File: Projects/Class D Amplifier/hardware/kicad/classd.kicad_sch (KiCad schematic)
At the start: 61 parts, among them J1 PWR IN 12V, J2 LINE IN, J3 SPEAKER 4R, Q1 IRF540N, Q2 IRF540N, Q3 IRF540N, Q4 IRF540N, U1 TL074, U2 LM311, U3 LM311, U4 LM311, U5 CD4049UBE, U6 HIP4082IPZ

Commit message: Class D amp: assign footprints, move to A2, and fix the sub crossover netclass
Every part now carries a through-hole footprint chosen for isolation milling
with an 0.8 mm end mill. The sheet moves to A2 to match how the board is being
drawn, and the layout script emits that so regenerating cannot revert it.

Footprints were audited for their smallest pad-to-pad gap before assignment,
because a gap narrower than the tool is never isolated and ships as a short.
Two stock picks failed that test. The Alps RK09K pot is 0.70 mm and cannot be
built, so the level control uses the ACP CA14V-15 with its 5 mm pin pitch
instead - the shop only specifies "10k", so measure the real part before
cutting copper. The stock TO-220 is 0.64 mm, so the bridge FETs use the
narrowed-pad variant at 0.84 mm; that clears the tool but sits under the
netclass clearance, so classd.kicad_dru relaxes it for those four parts and
nothing else. Everything else is 0.94 mm or wider.

The bornier terminal blocks and the mill-specific TO-220, LED and hand-wound
toroid footprints are vendored into lib/ and registered in fp-lib-table, since
KiCad 10 ships none of them.

subxo.kicad_pro gets the same netclass wire_width fix as this board. Its
Default class had no wire_width either, which is what makes KiCad 10 draw
every schematic wire at zero width and drop all the junction dots.
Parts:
- C1: footprint (none) -> Capacitor_THT:CP_Radial_D8.0mm_P3.50mm
- C10, C11, C12, C2, C5, C6, C7, C8, C9: footprint (none) -> Capacitor_THT:C_Disc_D5.0mm_W2.5mm_P5.00mm
- C13: footprint (none) -> Capacitor_THT:C_Rect_L16.5mm_W5.0mm_P15.00mm_MKT
- C14: footprint (none) -> Capacitor_THT:C_Rect_L7.0mm_W3.5mm_P5.00mm
- C3: footprint (none) -> Capacitor_THT:C_Rect_L13.0mm_W5.0mm_P10.00mm_FKS3_FKP3_MKS4
- C4: footprint (none) -> Capacitor_THT:CP_Radial_D18.0mm_P7.50mm
- D1: footprint (none) -> energy_system:LED_D3.0mm_P5.08mm_LaserPads
- D2, D3: footprint (none) -> Diode_THT:D_DO-41_SOD81_P10.16mm_Horizontal
- J1, J2, J3: footprint (none) -> TerminalBlock:TerminalBlock_bornier-2_P5.08mm
- L1, L2: footprint (none) -> energy_system:L_Toroid_Vertical_L34.5mm_W15.0mm_P28.20mm_LaserPads
- Q1, Q2, Q3, Q4: footprint (none) -> energy_system:TO-220-3_Vertical_LaserPads
- R1, R10, R11, R12, R13, R14, R15, R16, R17, R18, R19, R2, R20, R21, R3, R4, R5, R6, R7, R8, R9: footprint (none) -> Resistor_THT:R_Axial_DIN0207_L6.3mm_D2.5mm_P7.62mm_Horizontal
- R22: footprint (none) -> Resistor_THT:R_Axial_Power_L25.0mm_W9.0mm_P30.48mm
- RV1: footprint (none) -> Potentiometer_THT:Potentiometer_Bourns_3296W_Vertical
- RV2: footprint (none) -> Potentiometer_THT:Potentiometer_ACP_CA14V-15_Vertical
- TP1, TP2, TP3, TP4, TP5: footprint (none) -> TestPoint:TestPoint_THTPad_2.5x2.5mm_Drill1.2mm
- U1: footprint (none) -> Package_DIP:DIP-14_W7.62mm_LongPads
- U2, U3, U4: footprint (none) -> Package_DIP:DIP-8_W7.62mm_LongPads
- U5, U6: footprint (none) -> Package_DIP:DIP-16_W7.62mm_LongPads

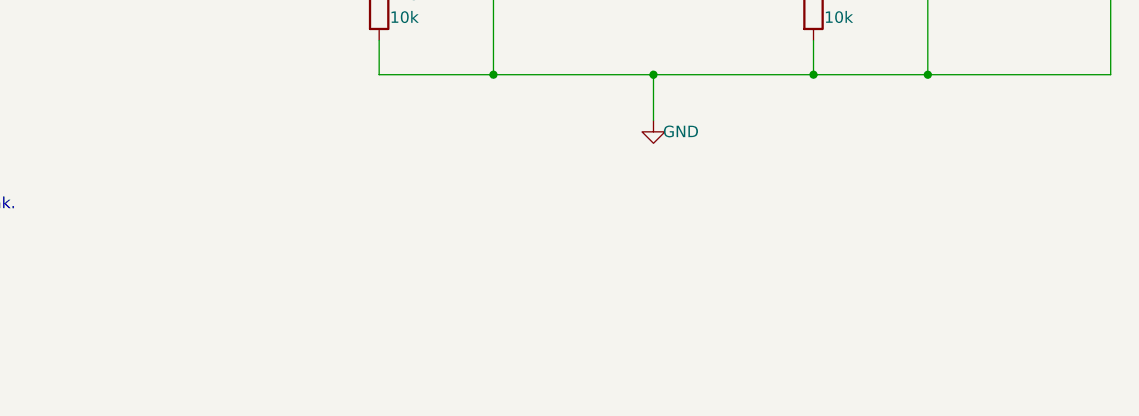
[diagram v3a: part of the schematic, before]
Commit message: Class D amp: link the testbenches from the board sheet, both ways
The board schematic now carries a SIMULATION index in the free space below the
bridge: one clickable line per testbench, opening that testbench's project.
Each testbench carries a link back to the board.

These are hyperlinks, not hierarchical sheets, and that was not the first
choice - it is the result of trying the obvious thing and measuring what it
did. Attaching sim_b_triangle to classd.kicad_sch as a hierarchical sheet and
exporting the netlist showed three separate kinds of damage: the testbench's
12 V source welded straight onto the board's +12V rail, taking it from 23 pins
to 25; the sim's sources landing in the board netlist ready for Update PCB
from Schematic to push them onto copper; and worst, the sim sheet's U1, R4 and
R5 silently merging with the board parts of the same name, quietly rewiring
real components. A hierarchy is one electrical design, so anything inside it
is part of the board whether you meant it or not.

Getting the hyperlink right took measuring too. KiCad 10 refuses to load a
schematic where the link is spelled (hyperlink ...) as it is on the PCB, or
where it sits beside (uuid ...) rather than inside (effects ...). It also
rejects an href that is a bare relative path or a ${KIPRJMOD} variable, but
accepts a relative path carrying the file: scheme - which is what is used, so
the links survive the repository being checked out anywhere.

Also fixed while here: labels that sat beside a wire end rather than on it
left dangling endpoints, and the testbench supplies needed a ground PWR_FLAG
as well as a rail one. All four sheets now pass ERC with zero violations, and
the simulation checks still pass 16/16.
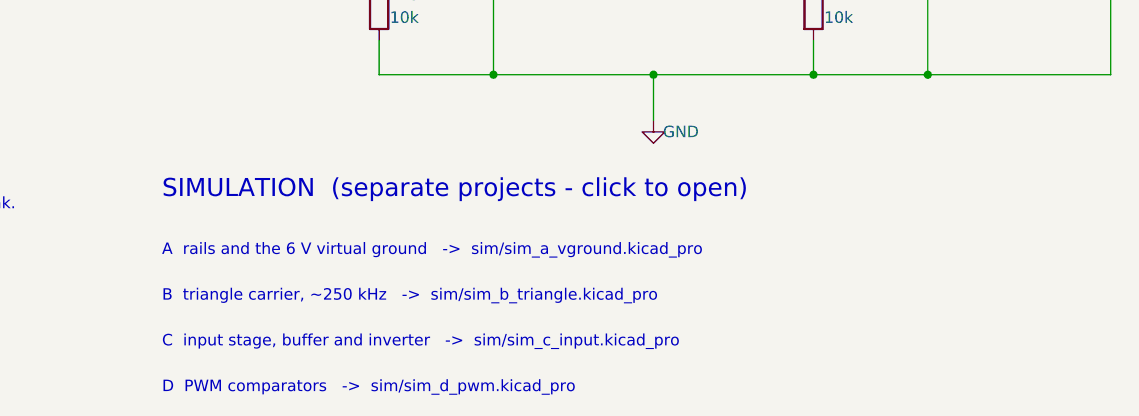
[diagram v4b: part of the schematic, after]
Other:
- note added: "A rails and the 6 V virtual ground -> sim/sim_a_vground.kicad_pro"
- note added: "B triangle carrier, ~250 kHz -> sim/sim_b_triangle.kicad_pro"
- note added: "C input stage, buffer and inverter -> sim/sim_c_input.kicad_pro"
- note added: "D PWM comparators -> sim/sim_d_pwm.kicad_pro"
- note added: "SIMULATION (separate projects - click to open)"
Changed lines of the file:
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@@
+		)
+	)
+	(text "SIMULATION  (separate projects - click to open)"
+		(at 317.5 374.65 0)
+		(effects
+			(font
+				(size 2 2)
+			)
+			(justify left bottom)
+		)
+	)
+	(text "A  rails and the 6 V virtual ground   ->  sim/sim_a_vground.kicad_pro"
+		(at 317.5 381 0)
+		(effects
+			(font
+				(size 1.27 1.27)
+			)
+			(justify left bottom)
+			(href "file:sim/sim_a_vground.kicad_pro")
+		)
+	)
+	(text "B  triangle carrier, ~250 kHz   ->  sim/sim_b_triangle.kicad_pro"
+		(at 317.5 386.08 0)
+		(effects
+			(font
+				(size 1.27 1.27)
+			)
+			(justify left bottom)
+			(href "file:sim/sim_b_triangle.kicad_pro")
+		)
+	)
+	(text "C  input stage, buffer and inverter   ->  sim/sim_c_input.kicad_pro"
+		(at 317.5 391.16 0)
+		(effects
+			(font
+				(size 1.27 1.27)
+			)
+			(justify left bottom)
+			(href "file:sim/sim_c_input.kicad_pro")
+		)
+	)
+	(text "D  PWM comparators   ->  sim/sim_d_pwm.kicad_pro"
+		(at 317.5 396.24 0)
+		(effects
+			(font
+				(size 1.27 1.27)
+			)
+			(justify left bottom)
+			(href "file:sim/sim_d_pwm.kicad_pro")
 		)
 	)

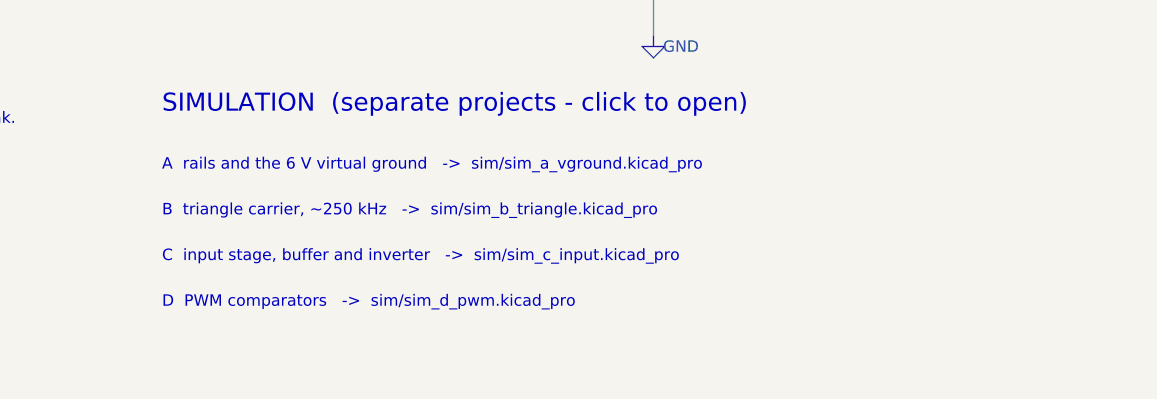
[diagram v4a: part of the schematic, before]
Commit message: Class D amp: the remaining three testbenches, E, F and G
E drives the CD4049 complement chain into the HIP4082 and measures what the
dead-time resistor actually buys: 225 ns with both gates off, never both on,
and a bootstrap that fills in ~50 us and settles one Schottky drop below the
rail. The switch nodes need holding down for that -- left floating they drift
up through the driver's own leakage until the bootstrap caps have barely a
volt across them, so R23/R24 stand in for the low-side FET being on.

F puts four real IRF540N cards, body diode included, under the driver and runs
them into the LC filter and a 4 ohm load at a fixed 79/21 duty: 11.75 W with
0.28 Vpp of carrier left on the output.

G is the whole chain, audio in to speaker out, and it is the one that answers
the design question. It makes 13 W -- and at that level AUDIO_P bottoms out at
4.00 V, which is the TL074's input common-mode floor. Full output and the
input stage's limit coincide exactly; there is no headroom to trade. That was
flagged on paper in the build notes and is now a number the harness asserts.

Three fixes fell out of building them, all in code that had never been
exercised because no bench used it before:

- the IRF540N Sim.Pins map said 1=D 2=G, but the symbol numbers its pins to
  the TO-220 pinout, 1=G 2=D. The bridge would have simulated as four
  transistors wired gate to drain.
- KiCad validates every Sim.Params key against the subcircuit's own parameter
  list and refuses the netlist export for one it cannot find, so the HIP4082's
  dead time moves from an internal .param to the .subckt line.
- a sym-lib-table registers the vendored CD4049 symbol, clearing the
  lib_symbol_issues ERC violations on every sheet that uses it.

The driver, bridge and filter are now drawn once and translated onto the three
sheets, with the geometry taken from the matching block of the board's own
layout script -- a bootstrap wired one way on the board and another way in its
testbench proves nothin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
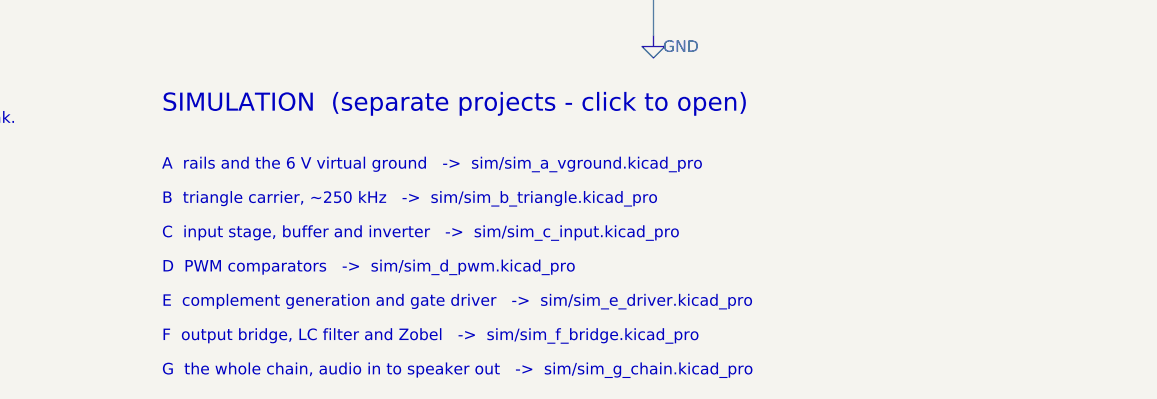
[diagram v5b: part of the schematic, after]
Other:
- note added: "E complement generation and gate driver -> sim/sim_e_driver.kicad_pro"
- note added: "F output bridge, LC filter and Zobel -> sim/sim_f_bridge.kicad_pro"
- note added: "G the whole chain, audio in to speaker out -> sim/sim_g_chain.kicad_pro"
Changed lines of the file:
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@@
 	)
 	(text "B  triangle carrier, ~250 kHz   ->  sim/sim_b_triangle.kicad_pro"
-		(at 317.5 386.08 0)
+		(at 317.5 384.81 0)
 		(effects
 			(font
@@
 	)
 	(text "C  input stage, buffer and inverter   ->  sim/sim_c_input.kicad_pro"
-		(at 317.5 391.16 0)
+		(at 317.5 388.62 0)
 		(effects
 			(font
@@
 	)
 	(text "D  PWM comparators   ->  sim/sim_d_pwm.kicad_pro"
-		(at 317.5 396.24 0)
+		(at 317.5 392.43 0)
 		(effects
 			(font
@@
 		)
 	)
+	(text "E  complement generation and gate driver   ->  sim/sim_e_driver.kicad_pro"
+		(at 317.5 396.24 0)
+		(effects
+			(font
+				(size 1.27 1.27)
+			)
+			(justify left bottom)
+			(href "file:sim/sim_e_driver.kicad_pro")
+		)
+	)
+	(text "F  output bridge, LC filter and Zobel   ->  sim/sim_f_bridge.kicad_pro"
+		(at 317.5 400.05 0)
+		(effects
+			(font
+				(size 1.27 1.27)
+			)
+			(justify left bottom)
+			(href "file:sim/sim_f_bridge.kicad_pro")
+		)
+	)
+	(text "G  the whole chain, audio in to speaker out   ->  sim/sim_g_chain.kicad_pro"
+		(at 317.5 403.86 0)
+		(effects
+			(font
+				(size 1.27 1.27)
+			)
+			(justify left bottom)
+			(href "file:sim/sim_g_chain.kicad_pro")
+		)
+	)

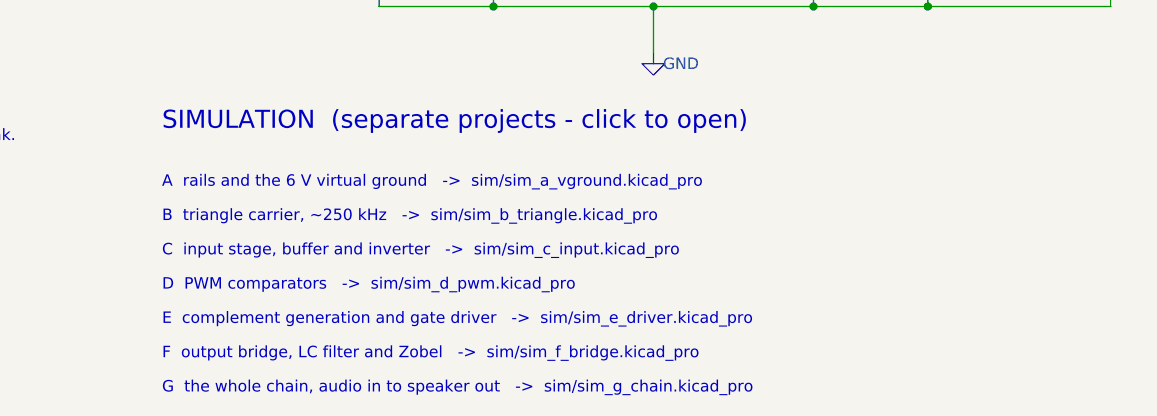
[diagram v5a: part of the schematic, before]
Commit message: Class D amp: point the simulation links at the sheets, not the projects
Clicking a link opened the project manager and left you one click short of
the drawing. Windows resolves the two extensions to different programs:

  .kicad_pro -> kicad.exe     the project manager
  .kicad_sch -> eeschema.exe  the schematic editor, straight onto the sheet

So the board's index and the benches' back-links now name the .kicad_sch.
Eeschema still picks up the matching .kicad_pro sitting beside it, which is
what carries the netclass and the simulator workbook, so nothing is lost by
skipping the project manager.

Note for anyone setting this up on another machine: the association has to
point at the KiCad version the files were written with. On this PC
.kicad_sch resolved to the 9.0 eeschema while .kicad_pro resolved to 10.0,
and a 9.0 editor cannot open a 10.0 schematic.
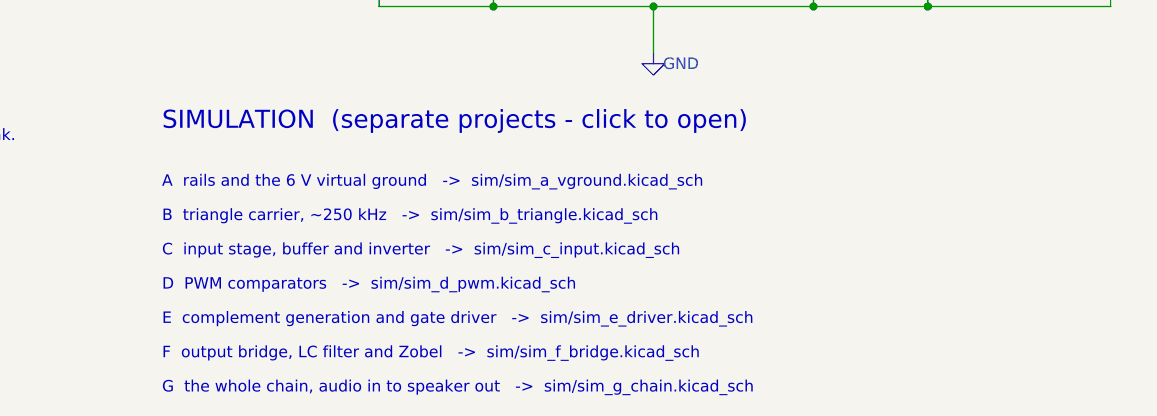
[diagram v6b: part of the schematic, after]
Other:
- note added: "A rails and the 6 V virtual ground -> sim/sim_a_vground.kicad_sch"
- note added: "B triangle carrier, ~250 kHz -> sim/sim_b_triangle.kicad_sch"
- note added: "C input stage, buffer and inverter -> sim/sim_c_input.kicad_sch"
- note added: "D PWM comparators -> sim/sim_d_pwm.kicad_sch"
- note added: "E complement generation and gate driver -> sim/sim_e_driver.kicad_sch"
- note added: "F output bridge, LC filter and Zobel -> sim/sim_f_bridge.kicad_sch"
- note added: "G the whole chain, audio in to speaker out -> sim/sim_g_chain.kicad_sch"
- note removed: "A rails and the 6 V virtual ground -> sim/sim_a_vground.kicad_pro"
- note removed: "B triangle carrier, ~250 kHz -> sim/sim_b_triangle.kicad_pro"
- note removed: "C input stage, buffer and inverter -> sim/sim_c_input.kicad_pro"
- note removed: "D PWM comparators -> sim/sim_d_pwm.kicad_pro"
- note removed: "E complement generation and gate driver -> sim/sim_e_driver.kicad_pro"
- note removed: "F output bridge, LC filter and Zobel -> sim/sim_f_bridge.kicad_pro"
- note removed: "G the whole chain, audio in to speaker out -> sim/sim_g_chain.kicad_pro"
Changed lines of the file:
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@@
 		)
 	)
-	(text "A  rails and the 6 V virtual ground   ->  sim/sim_a_vground.kicad_pro"
+	(text "A  rails and the 6 V virtual ground   ->  sim/sim_a_vground.kicad_sch"
 		(at 317.5 381 0)
 		(effects
@@
 			)
 			(justify left bottom)
-			(href "file:sim/sim_a_vground.kicad_pro")
+			(href "file:sim/sim_a_vground.kicad_sch")
 		)
 	)
-	(text "B  triangle carrier, ~250 kHz   ->  sim/sim_b_triangle.kicad_pro"
+	(text "B  triangle carrier, ~250 kHz   ->  sim/sim_b_triangle.kicad_sch"
 		(at 317.5 384.81 0)
 		(effects
@@
 			)
 			(justify left bottom)
-			(href "file:sim/sim_b_triangle.kicad_pro")
+			(href "file:sim/sim_b_triangle.kicad_sch")
 		)
 	)
-	(text "C  input stage, buffer and inverter   ->  sim/sim_c_input.kicad_pro"
+	(text "C  input stage, buffer and inverter   ->  sim/sim_c_input.kicad_sch"
 		(at 317.5 388.62 0)
 		(effects
@@
 			)
 			(justify left bottom)
-			(href "file:sim/sim_c_input.kicad_pro")
+			(href "file:sim/sim_c_input.kicad_sch")
 		)
 	)
-	(text "D  PWM comparators   ->  sim/sim_d_pwm.kicad_pro"
+	(text "D  PWM comparators   ->  sim/sim_d_pwm.kicad_sch"
 		(at 317.5 392.43 0)
 		(effects
@@
 			)
 			(justify left bottom)
-			(href "file:sim/sim_d_pwm.kicad_pro")
+			(href "file:sim/sim_d_pwm.kicad_sch")
 		)
 	)
-	(text "E  complement generation and gate driver   ->  sim/sim_e_driver.kicad_pro"
+	(text "E  complement generation and gate driver   ->  sim/sim_e_driver.kicad_sch"
 		(at 317.5 396.24 0)
 		(effects
@@
 			)
 			(justify left bottom)
-			(href "file:sim/sim_e_driver.kicad_pro")
+			(href "file:sim/sim_e_driver.kicad_sch")
 		)
 	)
-	(text "F  output bridge, LC filter and Zobel   ->  sim/sim_f_bridge.kicad_pro"
+	(text "F  output bridge, LC filter and Zobel   ->  sim/sim_f_bridge.kicad_sch"
 		(at 317.5 400.05 0)
 		(effects
@@
 			)
 			(justify left bottom)
-			(href "file:sim/sim_f_bridge.kicad_pro")
+			(href "file:sim/sim_f_bridge.kicad_sch")
 		)
 	)
-	(text "G  the whole chain, audio in to speaker out   ->  sim/sim_g_chain.kicad_pro"
+	(text "G  the whole chain, audio in to speaker out   ->  sim/sim_g_chain.kicad_sch"
 		(at 317.5 403.86 0)
 		(effects
@@
 			)
 			(justify left bottom)
-			(href "file:sim/sim_g_chain.kicad_pro")
+			(href "file:sim/sim_g_chain.kicad_sch")
 		)
 	)
